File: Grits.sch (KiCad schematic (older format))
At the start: 64 parts, among them J1 Conn_01x06_MountingPin, J2 Conn_02x01, J3 Conn_ARM_JTAG_SWD_10, J4 Conn_01x03, J5 Conn_01x04_MountingPin, J6 Conn_01x04_MountingPin, Q1 BUK7M9R9-60E, Q2 BUK7M9R9-60E, Q3 BUK7M9R9-60E, Q4 BUK7M9R9-60E, Q5 BUK7M9R9-60E, Q6 BUK7M9R9-60E, U1 STSPIN32F0B

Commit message: ✨ Add v1.1
Featuring rotated Hall connector going to different timer inputs
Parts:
- C_12V1: value 2.2µF -> 2.2µF/16V
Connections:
- net HALL_1_R: now also U1.11 (PA0); no longer U1.13 (PA2)
- net HALL_3_R: now also U1.13 (PA2); no longer U1.11 (PA0)
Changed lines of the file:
@@
 P 6400 1500
 F 0 "C_12V1" H 6515 1546 50  0000 L CNN
-F 1 "2.2µF" H 6515 1455 50  0000 L CNN
+F 1 "2.2µF/16V" H 6515 1455 50  0000 L CNN
 F 2 "Capacitor_SMD:C_0603_1608Metric" H 6438 1350 50  0001 C CNN
 F 3 "~" H 6400 1500 50  0001 C CNN
@@
 Wire Wire Line
 	3300 2600 4000 2600
-Text Label 3300 2600 0    50   ~ 0
+Text Label 3300 2400 0    50   ~ 0
 HALL_1_R
 Text Label 3300 2500 0    50   ~ 0
 HALL_2_R
-Text Label 3300 2400 0    50   ~ 0
+Text Label 3300 2600 0    50   ~ 0
 HALL_3_R
 Wire Wire Line

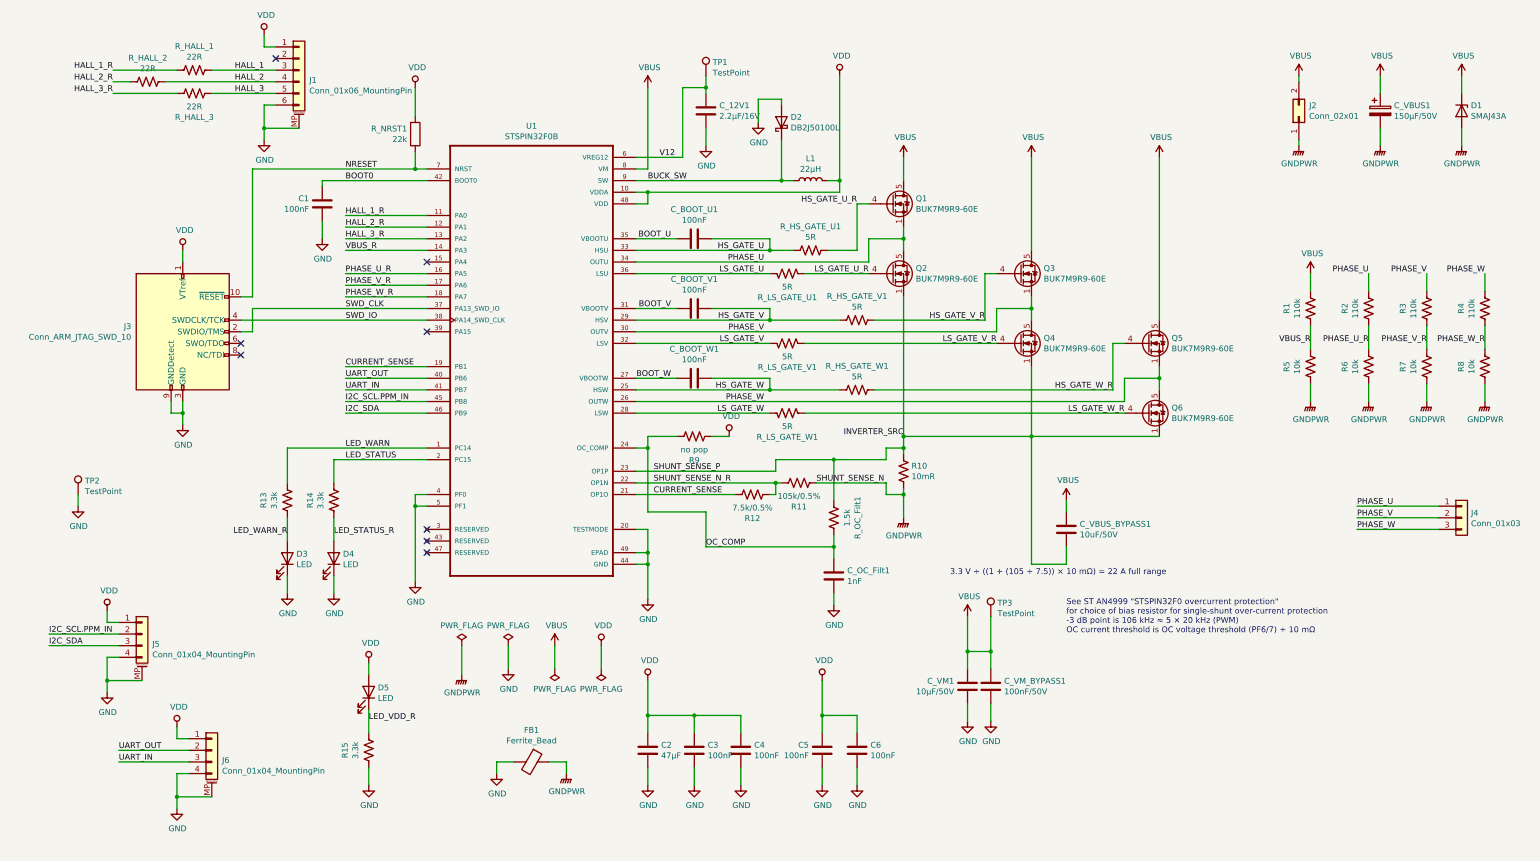
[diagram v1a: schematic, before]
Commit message: ✨ Add v1.3a (DFM)
v1.2: Retooled for DFM through JLCPCB
v1.3: Fix bootstrap capacitor wiring error
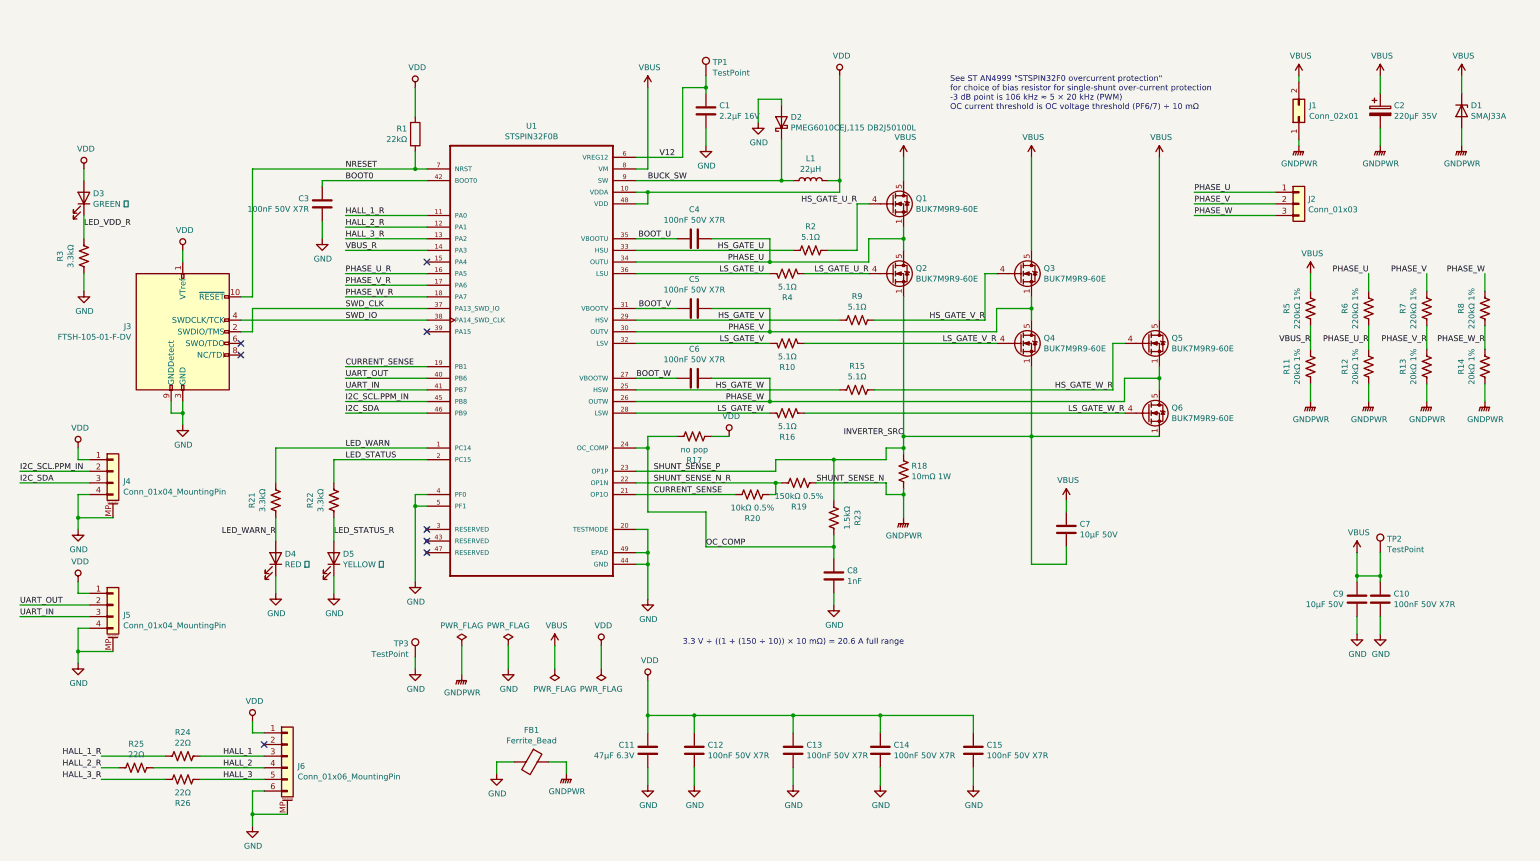
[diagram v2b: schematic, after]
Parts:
- removed R_LS_GATE_V1: 5R, Resistor_SMD:R_0603_1608Metric, symbol Device:R_US
- added R10: 5.1Ω, Resistor_SMD:R_0603_1608Metric, symbol Device:R_US
- C1: renamed from C_12V1; value 2.2µF/16V -> 2.2µF 16V
- C10: renamed from C_VM_BYPASS1; value 100nF/50V -> 100nF 50V X7R
- C11: renamed from C2; value 47µF -> 47µF 6.3V
- C12: renamed from C3; value 100nF -> 100nF 50V X7R
- C13: renamed from C4; value 100nF -> 100nF 50V X7R
- C14: renamed from C5; value 100nF -> 100nF 50V X7R
- C15: renamed from C6; value 100nF -> 100nF 50V X7R
- C2: renamed from C_VBUS1; value 150µF/50V -> 220µF 35V
- C3: renamed from C1; value 100nF -> 100nF 50V X7R
- C4: renamed from C_BOOT_U1; value 100nF -> 100nF 50V X7R
- C5: renamed from C_BOOT_V1; value 100nF -> 100nF 50V X7R
- C6: renamed from C_BOOT_W1; value 100nF -> 100nF 50V X7R
- C7: renamed from C_VBUS_BYPASS1; value 10uF/50V -> 10µF 50V
- C9: renamed from C_VM1; value 10µF/50V -> 10µF 50V
- D1: value SMAJ43A -> SMAJ33A
- D2: value DB2J50100L -> PMEG6010CEJ,115 DB2J50100L
- D3: renamed from D5; value LED -> GREEN 绿
- D4: renamed from D3; value LED -> RED 红
- D5: renamed from D4; value LED -> YELLOW 黄
- J3: value Conn_ARM_JTAG_SWD_10 -> FTSH-105-01-F-DV
- R1: renamed from R_NRST1; value 22k -> 22kΩ
- R11: renamed from R5; value 10k -> 20kΩ 1%
- R12: renamed from R6; value 10k -> 20kΩ 1%
- R13: renamed from R7; value 10k -> 20kΩ 1%
- R14: renamed from R8; value 10k -> 20kΩ 1%
- R15: renamed from R_HS_GATE_W1; value 5R -> 5.1Ω
- R16: renamed from R_LS_GATE_W1; value 5R -> 5.1Ω
- R18: renamed from R10; value 10mR -> 10mΩ 1W
- R19: renamed from R11; value 105k/0.5% -> 150kΩ 0.5%
- R2: renamed from R_HS_GATE_U1; value 5R -> 5.1Ω
- R20: renamed from R12; value 7.5k/0.5% -> 10kΩ 0.5%
- R21: renamed from R13; value 3.3k -> 3.3kΩ
- R22: renamed from R14; value 3.3k -> 3.3kΩ
- R23: renamed from R_OC_Filt1; value 1.5k -> 1.5kΩ
- R24: renamed from R_HALL_1; value 22R -> 22Ω
- R25: renamed from R_HALL_2; value 22R -> 22Ω
- R26: renamed from R_HALL_3; value 22R -> 22Ω
- R3: renamed from R15; value 3.3k -> 3.3kΩ
- R4: renamed from R_LS_GATE_U1; value 5R -> 5.1Ω
- R5: renamed from R1; value 110k -> 220kΩ 1%
- R6: renamed from R2; value 110k -> 220kΩ 1%
- R7: renamed from R3; value 110k -> 220kΩ 1%
- R8: renamed from R4; value 110k -> 220kΩ 1%
- R9: renamed from R_HS_GATE_V1; value 5R -> 5.1Ω
- renumbered C_OC_Filt1 to C8, J2 to J1, J4 to J2, J5 to J4, J6 to J5, J1 to J6, R9 to R17, TP3 to TP2, TP2 to TP3
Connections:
- net HS_GATE_U: no longer C4.1
- net HS_GATE_V: no longer C5.1
- net HS_GATE_W: no longer C6.1
- net LS_GATE_V: now also R10.2
- net LS_GATE_V_R: now also R10.1
- net PHASE_U: now also C4.1
- net PHASE_V: now also C5.1
- net PHASE_W: now also C6.1
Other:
- note added: "3.3 V ÷ ((1 + (150 ÷ 10)) × 10 mΩ) = 20.6 A full range"
- note removed: "3.3 V ÷ ((1 + (105 ÷ 7.5)) × 10 mΩ) = 22 A full range"
- moved on the sheet: C10, C13, C14, C15, C9, D3, D4, J2, J4, J5, J6, R21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
